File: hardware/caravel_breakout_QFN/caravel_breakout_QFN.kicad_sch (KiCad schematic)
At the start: 20 parts

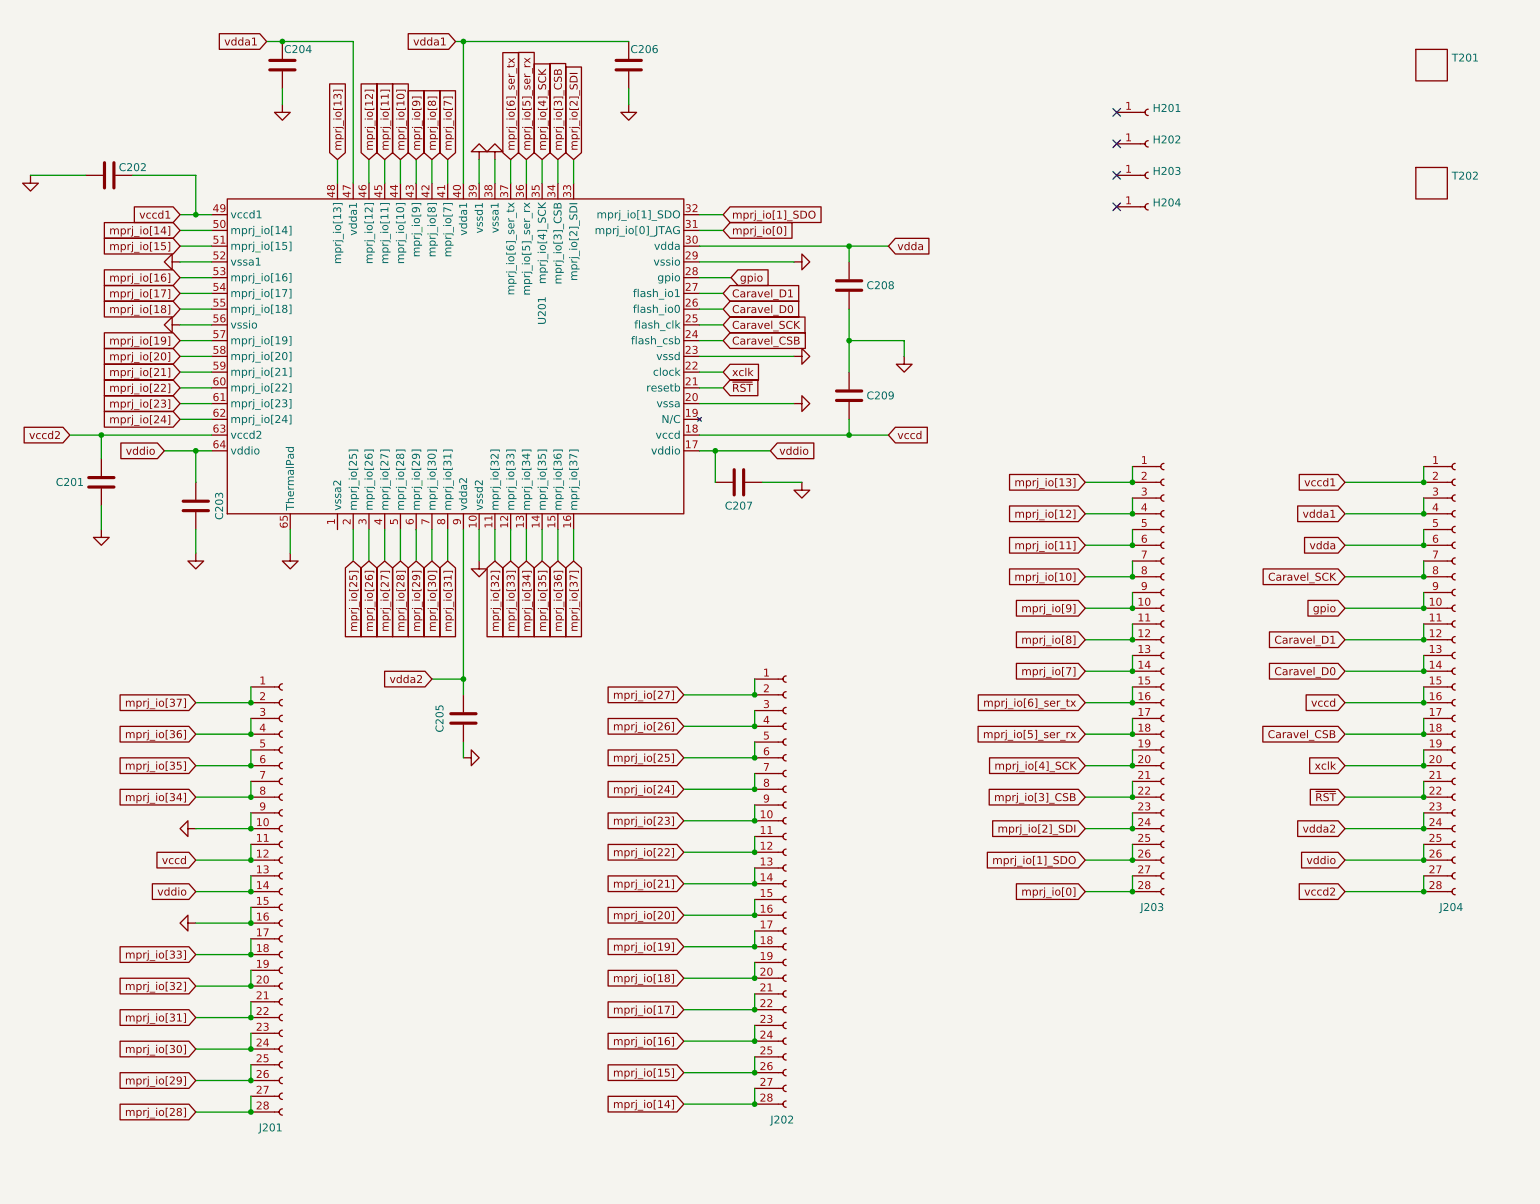
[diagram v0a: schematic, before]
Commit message: 
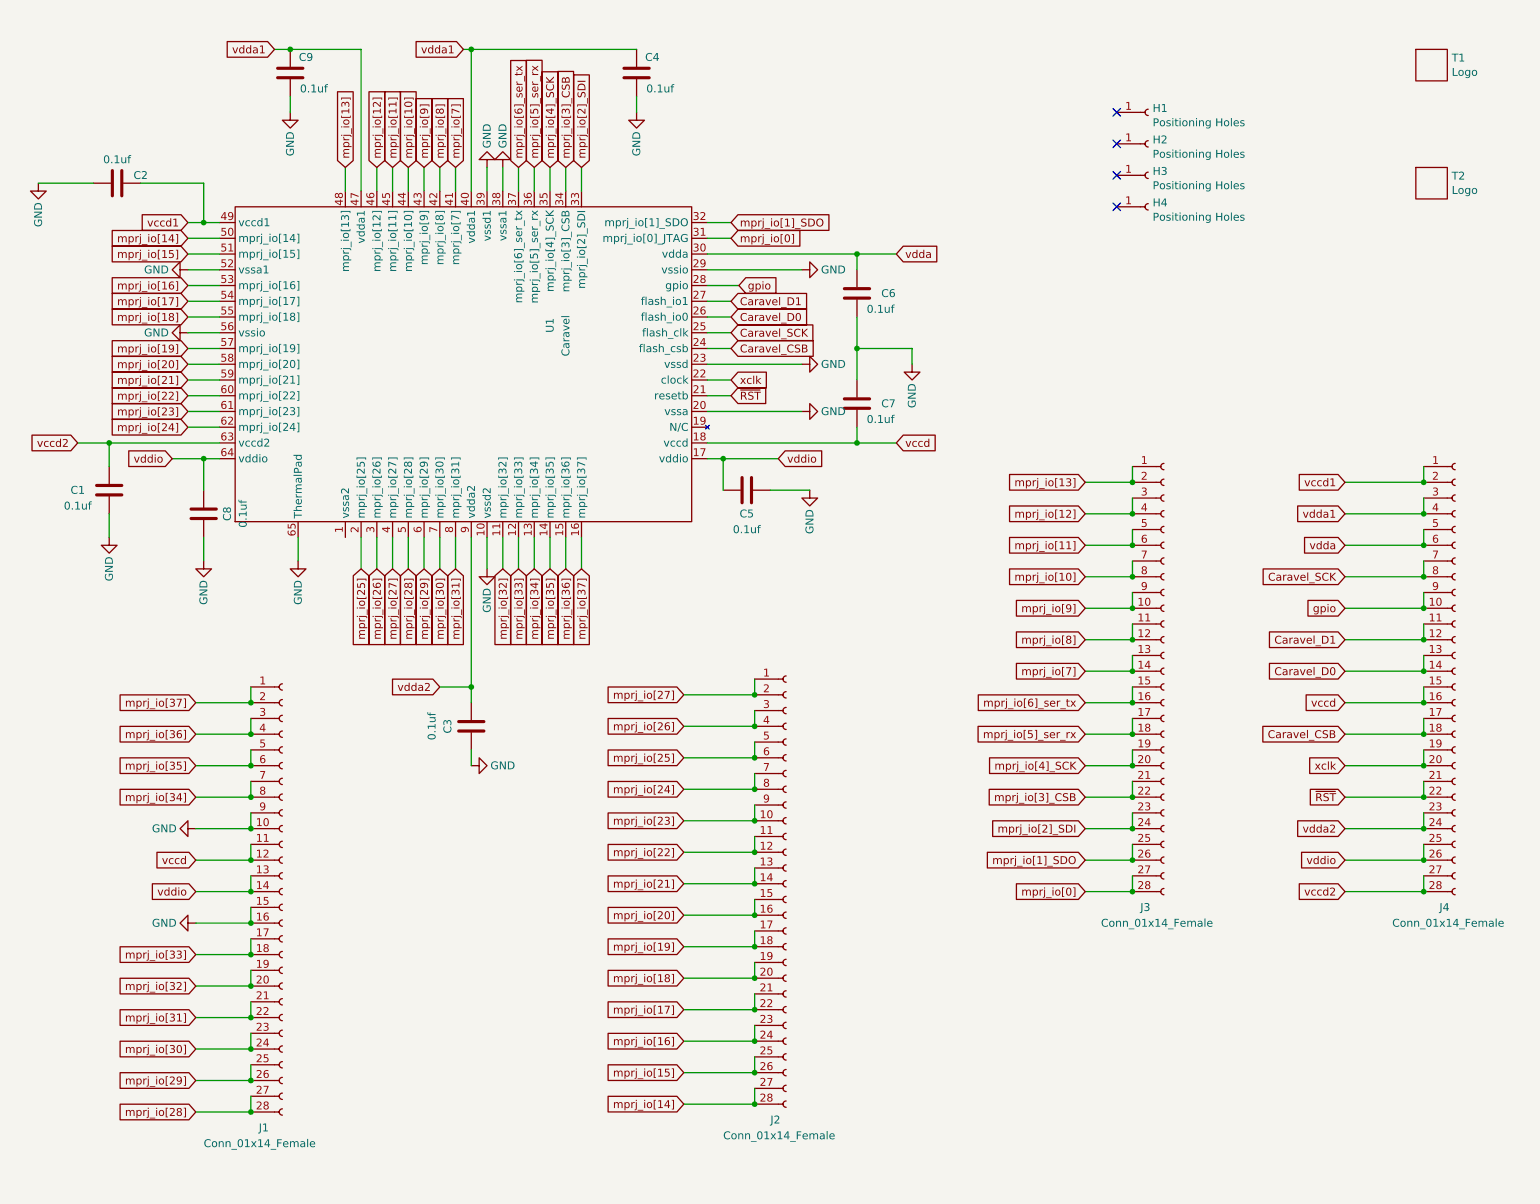
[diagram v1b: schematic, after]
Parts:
- removed C201, C202, C203, C204, C205, C206, C207, C208, C209: (no value), symbol Device:C
- removed U201: (no value), symbol Caravel_board:Caravel
- added C1, C2, C3, C4, C5, C6, C7, C8, C9: 0.1uf, Capacitor_SMD:C_0402_1005Metric, symbol Device:C
- added U1: Caravel, Package_DFN_QFN:QFN-64-1EP_9x9mm_P0.5mm_EP6x6mm, symbol Caravel_board:Caravel
- H1: renamed from H201; value (none) -> Positioning Holes; footprint (none) -> MountingHole:MountingHole_2.2mm_M2_ISO7380_Pad
- H2: renamed from H202; value (none) -> Positioning Holes; footprint (none) -> MountingHole:MountingHole_2.2mm_M2_ISO7380_Pad
- H3: renamed from H203; value (none) -> Positioning Holes; footprint (none) -> MountingHole:MountingHole_2.2mm_M2_ISO7380_Pad
- H4: renamed from H204; value (none) -> Positioning Holes; footprint (none) -> MountingHole:MountingHole_2.2mm_M2_ISO7380_Pad
- J1: renamed from J201; value (none) -> Conn_01x14_Female; footprint (none) -> Connector_PinHeader_1.27mm:PinHeader_2x14_P1.27mm_Vertical
- J2: renamed from J202; value (none) -> Conn_01x14_Female; footprint (none) -> Connector_PinHeader_1.27mm:PinHeader_2x14_P1.27mm_Vertical
- J3: renamed from J203; value (none) -> Conn_01x14_Female; footprint (none) -> Connector_PinHeader_1.27mm:PinHeader_2x14_P1.27mm_Vertical
- J4: renamed from J204; value (none) -> Conn_01x14_Female; footprint (none) -> Connector_PinHeader_1.27mm:PinHeader_2x14_P1.27mm_Vertical
- T1: renamed from T201; value (none) -> Logo; footprint (none) -> Caravel_Board:logo_small
- T2: renamed from T202; value (none) -> Logo; footprint (none) -> Caravel_Board:ef_logo
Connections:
- net Caravel_CSB: now also U1.24 (flash_csb)
- net Caravel_D0: now also U1.26 (flash_io0)
- net Caravel_D1: now also U1.27 (flash_io1)
- net Caravel_SCK: now also U1.25 (flash_clk)
- net GND: now also C1.1, C2.1, C3.1, C4.2, C5.1, C6.2, C7.1, C8.1, C9.2, U1.10 (vssd2), U1.20 (vssa), U1.23 (vssd), U1.29 (vssio), U1.38 (vssa1), U1.39 (vssd1), U1.52 (vssa1), U1.56 (vssio), U1.65 (ThermalPad)
- net gpio: now also U1.28 (gpio)
- net mprj_io[0]: now also U1.31 (mprj_io[0]_JTAG)
- net mprj_io[10]: now also U1.44 (mprj_io[10])
- net mprj_io[11]: now also U1.45 (mprj_io[11])
- net mprj_io[12]: now also U1.46 (mprj_io[12])
- net mprj_io[13]: now also U1.48 (mprj_io[13])
- net mprj_io[14]: now also U1.50 (mprj_io[14])
- net mprj_io[15]: now also U1.51 (mprj_io[15])
- net mprj_io[16]: now also U1.53 (mprj_io[16])
- net mprj_io[17]: now also U1.54 (mprj_io[17])
- net mprj_io[18]: now also U1.55 (mprj_io[18])
- net mprj_io[19]: now also U1.57 (mprj_io[19])
- net mprj_io[1]_SDO: now also U1.32 (mprj_io[1]_SDO)
- net mprj_io[20]: now also U1.58 (mprj_io[20])
- net mprj_io[21]: now also U1.59 (mprj_io[21])
- net mprj_io[22]: now also U1.60 (mprj_io[22])
- net mprj_io[23]: now also U1.61 (mprj_io[23])
- net mprj_io[24]: now also U1.62 (mprj_io[24])
- net mprj_io[25]: now also U1.2 (mprj_io[25])
- net mprj_io[26]: now also U1.3 (mprj_io[26])
- net mprj_io[27]: now also U1.4 (mprj_io[27])
- net mprj_io[28]: now also U1.5 (mprj_io[28])
- net mprj_io[29]: now also U1.6 (mprj_io[29])
- net mprj_io[2]_SDI: now also U1.33 (mprj_io[2]_SDI)
- net mprj_io[30]: now also U1.7 (mprj_io[30])
- net mprj_io[31]: now also U1.8 (mprj_io[31])
- net mprj_io[32]: now also U1.11 (mprj_io[32])
- net mprj_io[33]: now also U1.12 (mprj_io[33])
- net mprj_io[34]: now also U1.13 (mprj_io[34])
- net mprj_io[35]: now also U1.14 (mprj_io[35])
- net mprj_io[36]: now also U1.15 (mprj_io[36])
- net mprj_io[37]: now also U1.16 (mprj_io[37])
- net mprj_io[3]_CSB: now also U1.34 (mprj_io[3]_CSB)
- net mprj_io[4]_SCK: now also U1.35 (mprj_io[4]_SCK)
- net mprj_io[5]_ser_rx: now also U1.36 (mprj_io[5]_ser_rx)
- net mprj_io[6]_ser_tx: now also U1.37 (mprj_io[6]_ser_tx)
- net mprj_io[7]: now also U1.41 (mprj_io[7])
- net mprj_io[8]: now also U1.42 (mprj_io[8])
- net mprj_io[9]: now also U1.43 (mprj_io[9])
- net vccd: now also C7.2, U1.18 (vccd)
- net vccd1: now also C2.2, U1.49 (vccd1)
- net vccd2: now also C1.2, U1.63 (vccd2)
- net vdda: now also C6.1, U1.30 (vdda)
- net vdda1: now also C4.1, C9.1, U1.40 (vdda1), U1.47 (vdda1)
- net vdda2: now also C3.2, U1.9 (vdda2)
- net vddio: now also C5.2, C8.2, U1.17 (vddio), U1.64 (vddio)
- net xclk: now also U1.22 (clock)
- net ~{RST}: now also U1.21 (resetb)

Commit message: Updated the caravel QFN breakout board connectors
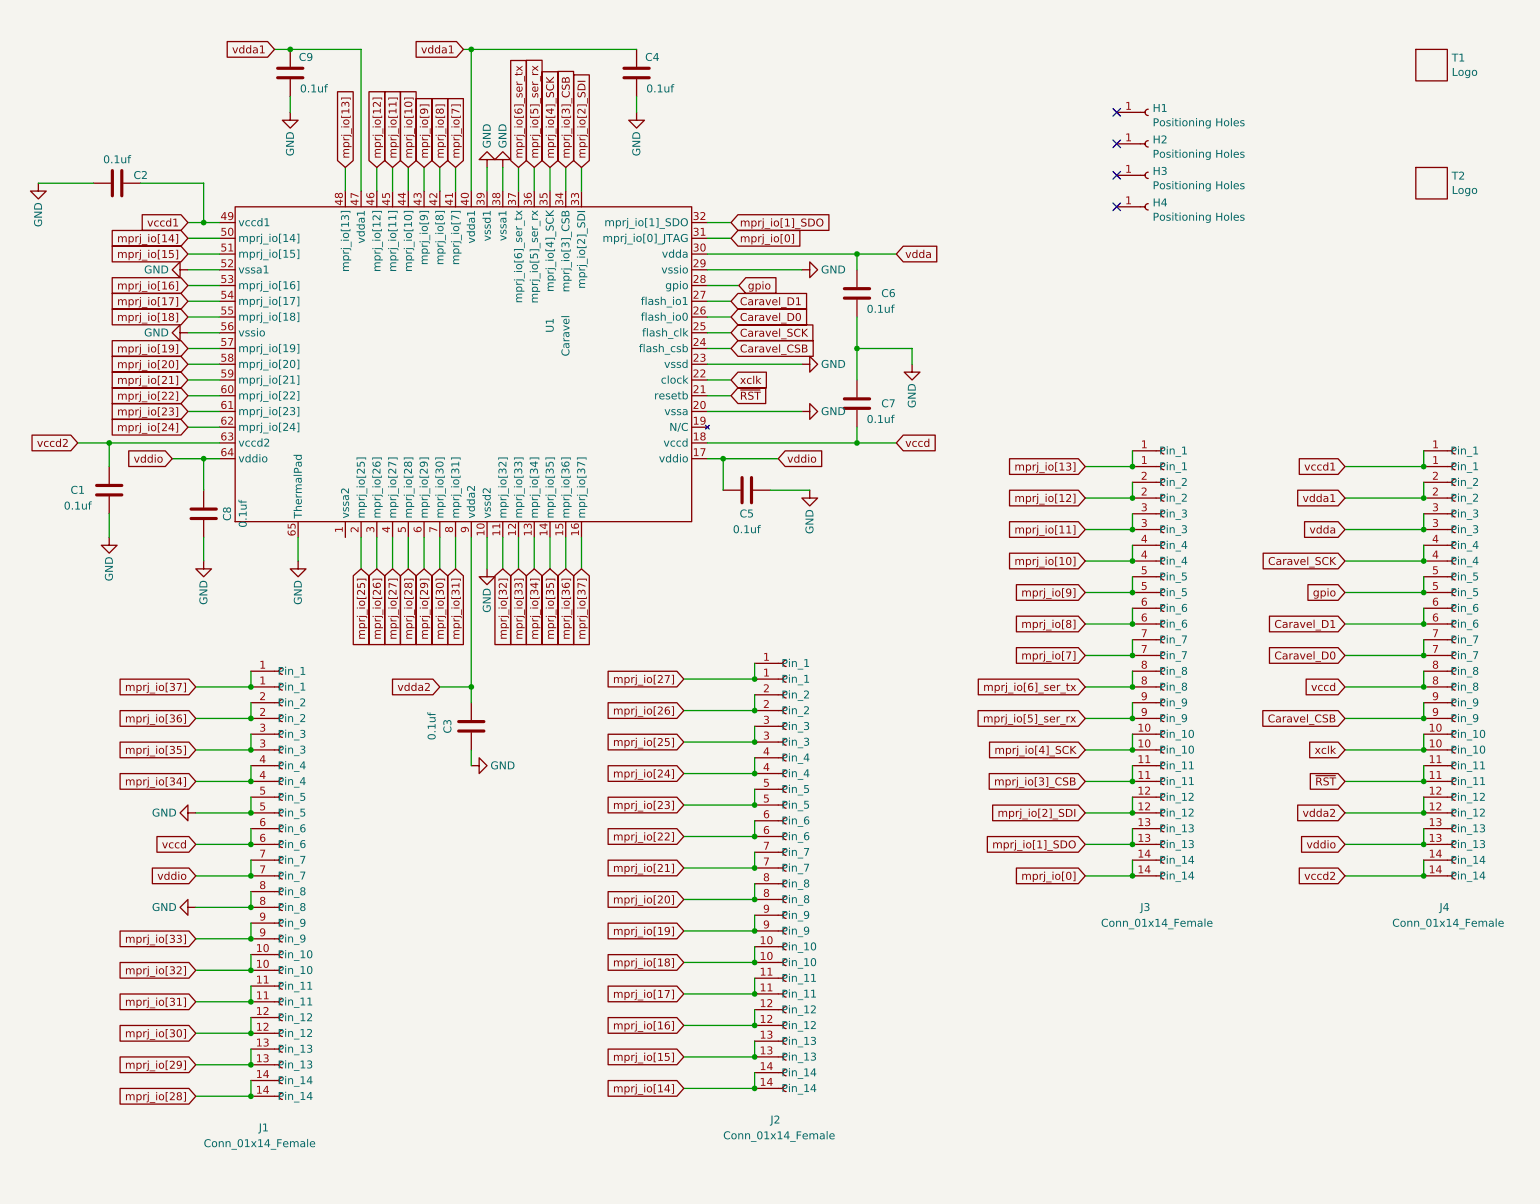
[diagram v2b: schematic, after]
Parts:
- J1, J2, J3, J4: footprint Connector_PinHeader_1.27mm:PinHeader_2x14_P1.27mm_Vertical -> Caravel_Board:Caravel_Breakout_Connectors_2x14; symbol Connector:Conn_01x28_Female -> Caravel_board:caravel_breakout_connectors_1x14
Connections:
- net Caravel_CSB: now also J4.9 (Pin_9); no longer J4.17 (Pin_17), J4.18 (Pin_18)
- net Caravel_D0: now also J4.7 (Pin_7); no longer J4.13 (Pin_13), J4.14 (Pin_14)
- net Caravel_D1: now also J4.6 (Pin_6); no longer J4.11 (Pin_11), J4.12 (Pin_12)
- net Caravel_SCK: now also J4.4 (Pin_4); no longer J4.7 (Pin_7), J4.8 (Pin_8)
- net GND: now also J1.5 (Pin_5), J1.8 (Pin_8); no longer J1.10 (Pin_10), J1.15 (Pin_15), J1.16 (Pin_16), J1.9 (Pin_9)
- net gpio: now also J4.5 (Pin_5); no longer J4.10 (Pin_10), J4.9 (Pin_9)
- net mprj_io[0]: now also J3.14 (Pin_14); no longer J3.27 (Pin_27), J3.28 (Pin_28)
- net mprj_io[10]: now also J3.4 (Pin_4); no longer J3.7 (Pin_7), J3.8 (Pin_8)
- net mprj_io[11]: now also J3.3 (Pin_3); no longer J3.5 (Pin_5), J3.6 (Pin_6)
- net mprj_io[12]: now also J3.2 (Pin_2); no longer J3.3 (Pin_3), J3.4 (Pin_4)
- net mprj_io[13]: no longer J3.2 (Pin_2)
- net mprj_io[14]: now also J2.14 (Pin_14); no longer J2.27 (Pin_27), J2.28 (Pin_28)
- net mprj_io[15]: now also J2.13 (Pin_13); no longer J2.25 (Pin_25), J2.26 (Pin_26)
- net mprj_io[16]: now also J2.12 (Pin_12); no longer J2.23 (Pin_23), J2.24 (Pin_24)
- net mprj_io[17]: now also J2.11 (Pin_11); no longer J2.21 (Pin_21), J2.22 (Pin_22)
- net mprj_io[18]: now also J2.10 (Pin_10); no longer J2.19 (Pin_19), J2.20 (Pin_20)
- net mprj_io[19]: now also J2.9 (Pin_9); no longer J2.17 (Pin_17), J2.18 (Pin_18)
- net mprj_io[1]_SDO: now also J3.13 (Pin_13); no longer J3.25 (Pin_25), J3.26 (Pin_26)
- net mprj_io[20]: now also J2.8 (Pin_8); no longer J2.15 (Pin_15), J2.16 (Pin_16)
- net mprj_io[21]: now also J2.7 (Pin_7); no longer J2.13 (Pin_13), J2.14 (Pin_14)
- net mprj_io[22]: now also J2.6 (Pin_6); no longer J2.11 (Pin_11), J2.12 (Pin_12)
- net mprj_io[23]: now also J2.5 (Pin_5); no longer J2.10 (Pin_10), J2.9 (Pin_9)
- net mprj_io[24]: now also J2.4 (Pin_4); no longer J2.7 (Pin_7), J2.8 (Pin_8)
- net mprj_io[25]: now also J2.3 (Pin_3); no longer J2.5 (Pin_5), J2.6 (Pin_6)
- net mprj_io[26]: now also J2.2 (Pin_2); no longer J2.3 (Pin_3), J2.4 (Pin_4)
- net mprj_io[27]: no longer J2.2 (Pin_2)
- net mprj_io[28]: now also J1.14 (Pin_14); no longer J1.27 (Pin_27), J1.28 (Pin_28)
- net mprj_io[29]: now also J1.13 (Pin_13); no longer J1.25 (Pin_25), J1.26 (Pin_26)
- net mprj_io[2]_SDI: now also J3.12 (Pin_12); no longer J3.23 (Pin_23), J3.24 (Pin_24)
- net mprj_io[30]: now also J1.12 (Pin_12); no longer J1.23 (Pin_23), J1.24 (Pin_24)
- net mprj_io[31]: now also J1.11 (Pin_11); no longer J1.21 (Pin_21), J1.22 (Pin_22)
- net mprj_io[32]: now also J1.10 (Pin_10); no longer J1.19 (Pin_19), J1.20 (Pin_20)
- net mprj_io[33]: now also J1.9 (Pin_9); no longer J1.17 (Pin_17), J1.18 (Pin_18)
- net mprj_io[34]: now also J1.4 (Pin_4); no longer J1.7 (Pin_7), J1.8 (Pin_8)
- net mprj_io[35]: now also J1.3 (Pin_3); no longer J1.5 (Pin_5), J1.6 (Pin_6)
- net mprj_io[36]: now also J1.2 (Pin_2); no longer J1.3 (Pin_3), J1.4 (Pin_4)
- net mprj_io[37]: no longer J1.2 (Pin_2)
- net mprj_io[3]_CSB: now also J3.11 (Pin_11); no longer J3.21 (Pin_21), J3.22 (Pin_22)
- net mprj_io[4]_SCK: now also J3.10 (Pin_10); no longer J3.19 (Pin_19), J3.20 (Pin_20)
- net mprj_io[5]_ser_rx: now also J3.9 (Pin_9); no longer J3.17 (Pin_17), J3.18 (Pin_18)
- net mprj_io[6]_ser_tx: now also J3.8 (Pin_8); no longer J3.15 (Pin_15), J3.16 (Pin_16)
- net mprj_io[7]: now also J3.7 (Pin_7); no longer J3.13 (Pin_13), J3.14 (Pin_14)
- net mprj_io[8]: now also J3.6 (Pin_6); no longer J3.11 (Pin_11), J3.12 (Pin_12)
- net mprj_io[9]: now also J3.5 (Pin_5); no longer J3.10 (Pin_10), J3.9 (Pin_9)
- net vccd: now also J1.6 (Pin_6), J4.8 (Pin_8); no longer J1.11 (Pin_11), J1.12 (Pin_12), J4.15 (Pin_15), J4.16 (Pin_16)
- net vccd1: no longer J4.2 (Pin_2)
- net vccd2: now also J4.14 (Pin_14); no longer J4.27 (Pin_27), J4.28 (Pin_28)
- net vdda: now also J4.3 (Pin_3); no longer J4.5 (Pin_5), J4.6 (Pin_6)
- net vdda1: now also J4.2 (Pin_2); no longer J4.3 (Pin_3), J4.4 (Pin_4)
- net vdda2: now also J4.12 (Pin_12); no longer J4.23 (Pin_23), J4.24 (Pin_24)
- net vddio: now also J1.7 (Pin_7), J4.13 (Pin_13); no longer J1.13 (Pin_13), J1.14 (Pin_14), J4.25 (Pin_25), J4.26 (Pin_26)
- net xclk: now also J4.10 (Pin_10); no longer J4.19 (Pin_19), J4.20 (Pin_20)
- net ~{RST}: now also J4.11 (Pin_11); no longer J4.21 (Pin_21), J4.22 (Pin_22)

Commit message: add gerber files
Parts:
- U1: footprint Package_DFN_QFN:QFN-64-1EP_9x9mm_P0.5mm_EP6x6mm -> Package_DFN_QFN:QFN-64-1EP_9x9mm_P0.5mm_EP7.65x7.65mm_ThermalVias
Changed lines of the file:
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@@
       (effects (font (size 1.27 1.27)) (justify left))
     )
-    (property "Footprint" "Package_DFN_QFN:QFN-64-1EP_9x9mm_P0.5mm_EP6x6mm" (id 2) (at 90.17 68.58 0)
+    (property "Footprint" "Package_DFN_QFN:QFN-64-1EP_9x9mm_P0.5mm_EP7.65x7.65mm_ThermalVias" (id 2) (at 90.17 68.58 0)
       (effects (font (size 1.27 1.27)) hide)
     )
@@
     )
     (path "/d18d03f1-62e2-4695-bfe6-4b05c8fd039a"
-      (reference "U1") (unit 1) (value "Caravel") (footprint "Package_DFN_QFN:QFN-64-1EP_9x9mm_P0.5mm_EP6x6mm")
-    )
-  )
+      (reference "U1") (unit 1) (value "Caravel") (footprint "Package_DFN_QFN:QFN-64-1EP_9x9mm_P0.5mm_EP7.65x7.65mm_ThermalVias")
+    )
+  )
